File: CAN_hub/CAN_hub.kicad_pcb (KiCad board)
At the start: 2 copper layers, 8 parts, among them J1 Conn_01x04_Male, J2 Conn_01x04_Male, J3 Conn_01x04_Male, J4 Conn_01x04_Male, J5 Conn_01x04_Male, J6 Conn_01x04_Male, J7 Conn_01x04_Male, J8 Conn_01x04_Male

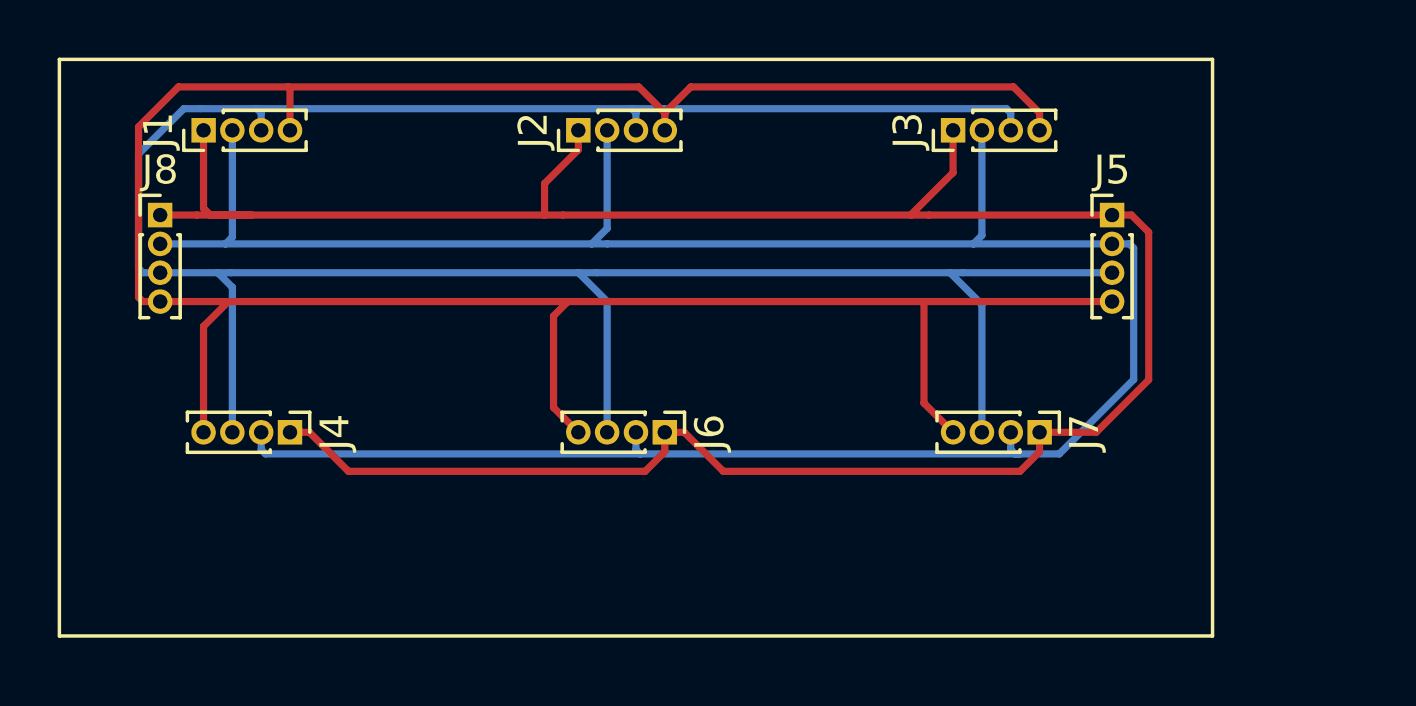
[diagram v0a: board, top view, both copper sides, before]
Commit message: Updated shematic and layout to accomodate changes from first round of testing
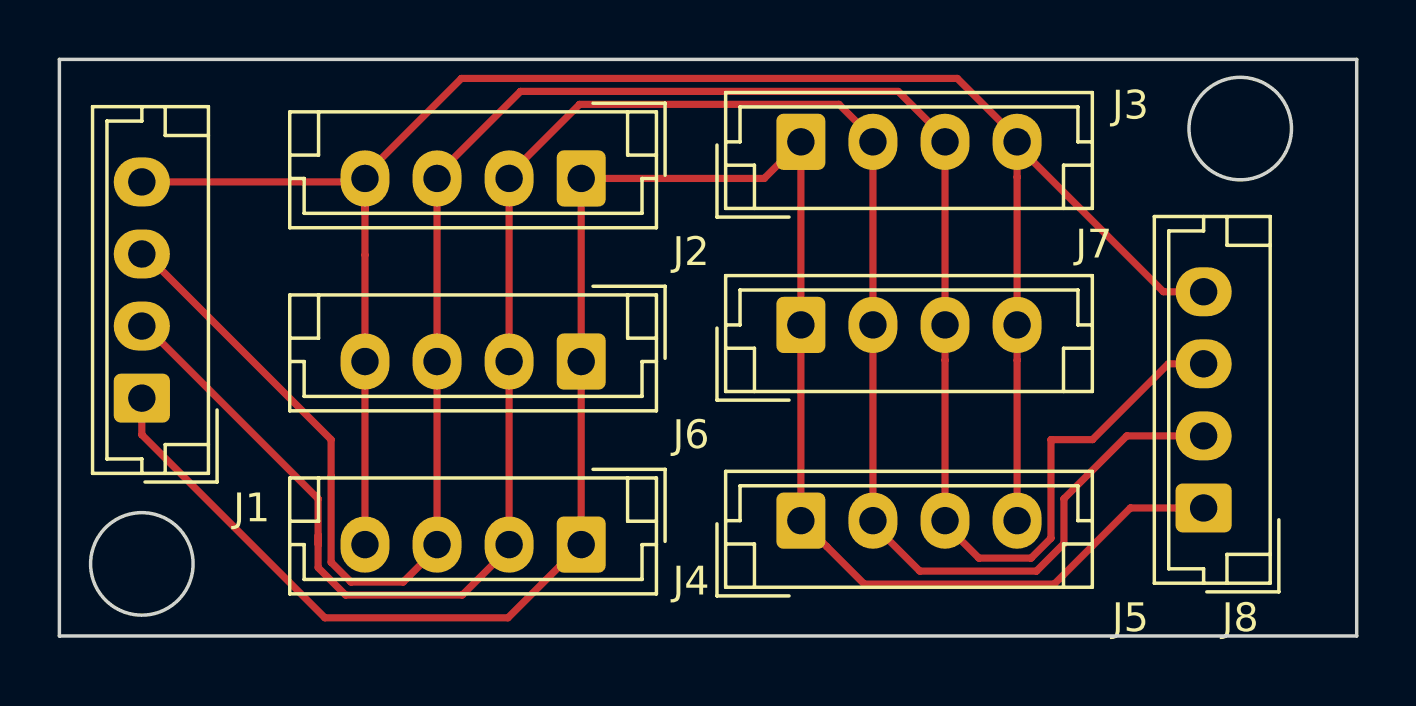
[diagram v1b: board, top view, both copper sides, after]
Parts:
- J1, J2, J3, J4, J5, J6, J7, J8: footprint Connector_PinHeader_1.00mm:PinHeader_1x04_P1.00mm_Vertical -> Connector_JST:JST_EH_B4B-EH-A_1x04_P2.50mm_Vertical
- moved J8 37.6 mm to (59.7, 35.6), turned to 90 degrees
- moved J5 15.1 mm to (45.7, 36.0)
- moved J4 10.8 mm to (38.1, 36.8), turned to 180 degrees
- moved J1 9.53 mm to (22.9, 31.8)
- moved J7 9.08 mm to (45.7, 29.2), turned to 0 degrees
- moved J3 5.30 mm to (45.7, 22.9), turned to 0 degrees
- moved J6 3.80 mm to (38.1, 30.5), turned to 180 degrees
- moved J2 1.67 mm to (38.1, 24.1), turned to 180 degrees
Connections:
- J1 pad 1: GND -> +5V
- J1 pad 2: CANH -> GND
- J1 pad 3: CANL -> CANH
- J1 pad 4: +5V -> CANL
- J2 pad 1: GND -> +5V
- J2 pad 2: CANH -> GND
- J2 pad 3: CANL -> CANH
- J2 pad 4: +5V -> CANL
- J3 pad 1: GND -> +5V
- J3 pad 2: CANH -> GND
- J3 pad 3: CANL -> CANH
- J3 pad 4: +5V -> CANL
- J4 pad 1: GND -> +5V
- J4 pad 2: CANH -> GND
- J4 pad 3: CANL -> CANH
- J4 pad 4: +5V -> CANL
- J5 pad 1: GND -> +5V
- J5 pad 2: CANH -> GND
- J5 pad 3: CANL -> CANH
- J5 pad 4: +5V -> CANL
- J6 pad 1: GND -> +5V
- J6 pad 2: CANH -> GND
- J6 pad 3: CANL -> CANH
- J6 pad 4: +5V -> CANL
- J7 pad 1: GND -> +5V
- J7 pad 2: CANH -> GND
- J7 pad 3: CANL -> CANH
- J7 pad 4: +5V -> CANL
- J8 pad 1: GND -> +5V
- J8 pad 2: CANH -> GND
- J8 pad 3: CANL -> CANH
- J8 pad 4: +5V -> CANL
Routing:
- net +5V: track 90.4 -> 70.2 mm
- net CANL: track 88.7 -> 69.2 mm
- net GND: track 84.7 -> 74.5 mm
- net CANH: track 84.4 -> 78.3 mm
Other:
- board outline added: 45 x 20 mm

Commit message: Finished layout and generated gerber files
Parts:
- moved J2 0.73 mm to (38.1, 23.4)
- moved J6 0.58 mm to (38.1, 29.9)
- moved J4 0.18 mm to (38.1, 36.6)
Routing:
- net +5V: track 70.2 -> 109.9 mm
- net GND: track 74.5 -> 107.4 mm
- net CANH: track 78.3 -> 65.5 mm
- net CANL: track 69.2 -> 70.2 mm
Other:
- net class Default: trace_width 0.25 -> 0.254
